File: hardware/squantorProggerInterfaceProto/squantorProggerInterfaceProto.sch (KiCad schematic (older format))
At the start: 2 parts

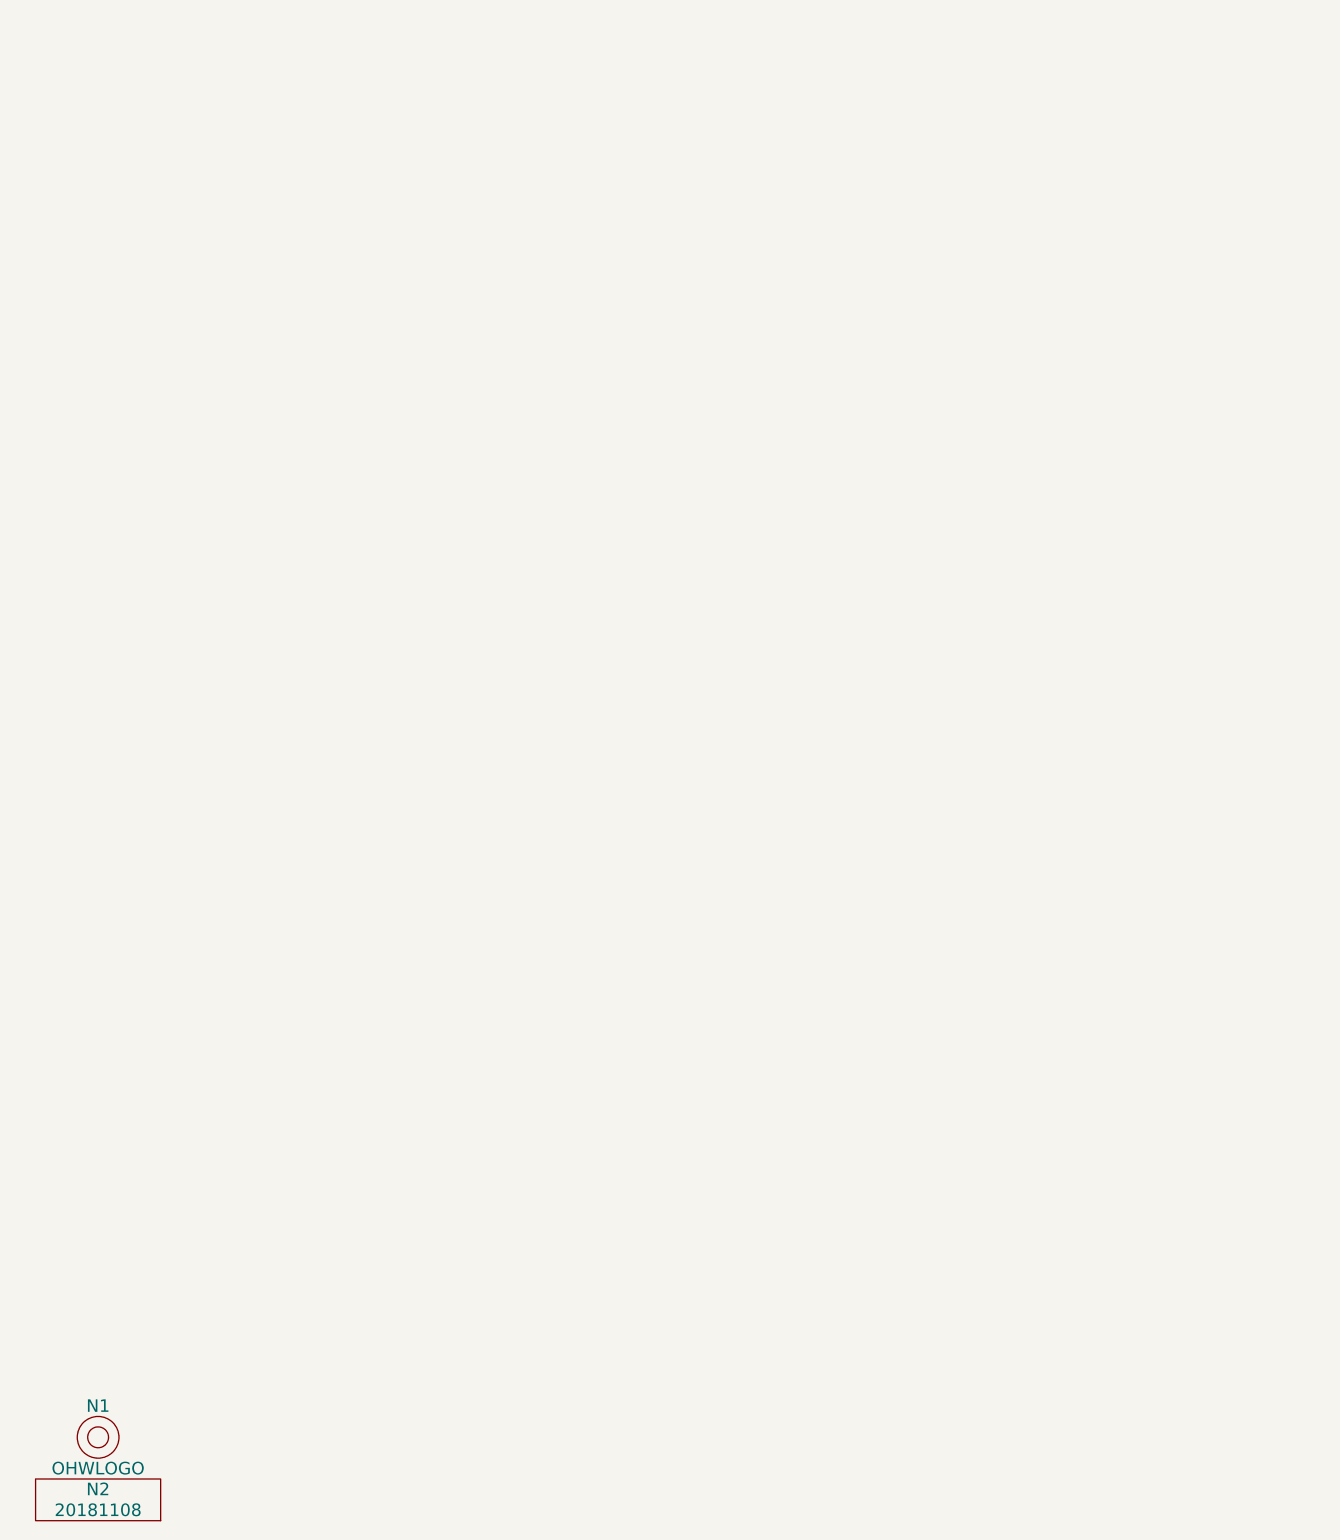
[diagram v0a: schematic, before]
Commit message: completed schematic, passes DRC
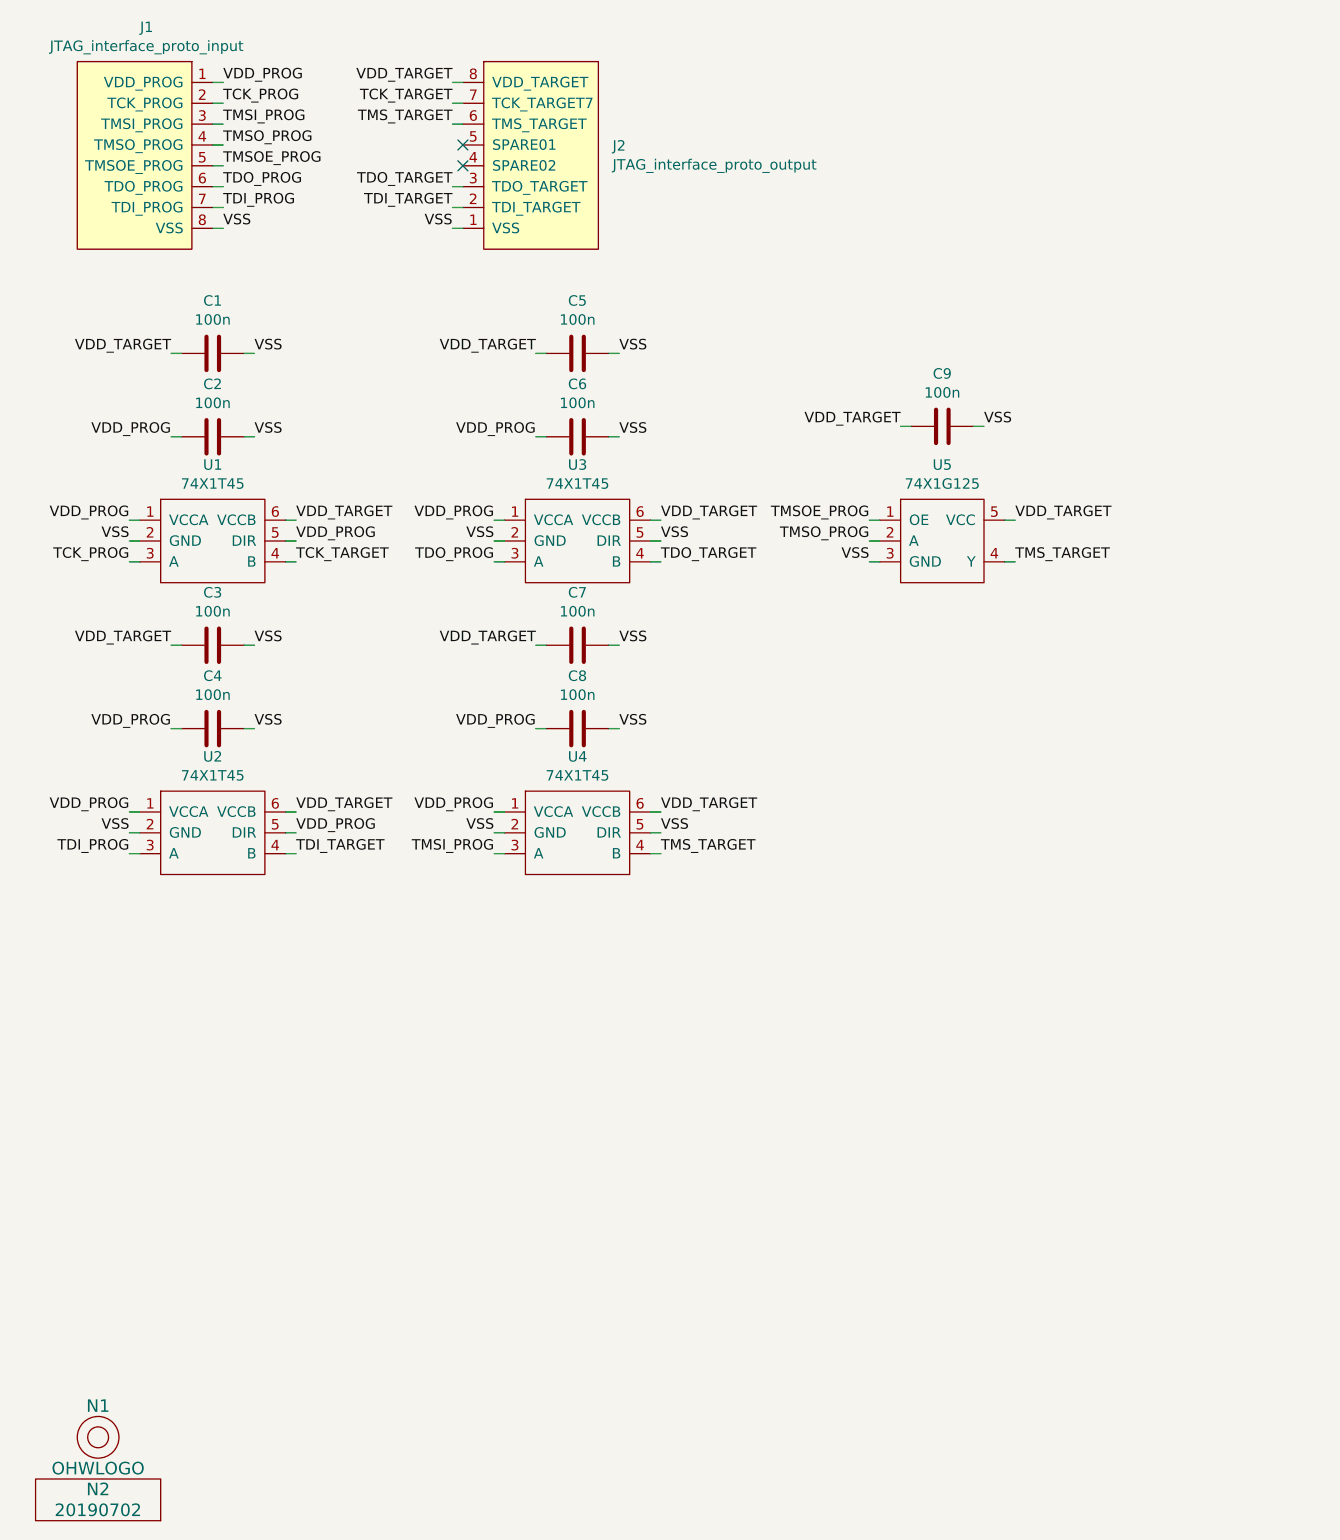
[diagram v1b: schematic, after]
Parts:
- added C1, C2, C3, C4, C5, C6, C7, C8, C9: 100n, SquantorRcl:C_0402, symbol Device:C
- added J1: JTAG_interface_proto_input, symbol SquantorConnectorsNamed:JTAG_interface_proto_input
- added J2: JTAG_interface_proto_output, symbol SquantorConnectorsNamed:JTAG_interface_proto_output
- added U1, U2, U3, U4: 74X1T45, symbol SquantorLogic:74X1T45
- added U5: 74X1G125, symbol SquantorLogic:74X1G125
- N2: value 20181108 -> 20190702
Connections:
- new net TCK_PROG: J1.2 (TCK_PROG), U1.3 (A)
- new net TCK_TARGET: J2.7 (TCK_TARGET7), U1.4 (B)
- new net TDI_PROG: J1.7 (TDI_PROG), U2.3 (A)
- new net TDI_TARGET: J2.2 (TDI_TARGET), U2.4 (B)
- new net TDO_PROG: J1.6 (TDO_PROG), U3.3 (A)
- new net TDO_TARGET: J2.3 (TDO_TARGET), U3.4 (B)
- new net TMSI_PROG: J1.3 (TMSI_PROG), U4.3 (A)
- new net TMSOE_PROG: J1.5 (TMSOE_PROG), U5.1 (OE)
- new net TMSO_PROG: J1.4 (TMSO_PROG), U5.2 (A)
- new net TMS_TARGET: J2.6 (TMS_TARGET), U4.4 (B), U5.4 (Y)
- new net VDD_PROG: C2.2, C4.2, C6.2, C8.2, J1.1 (VDD_PROG), U1.1 (VCCA), U1.5 (DIR), U2.1 (VCCA), U2.5 (DIR), U3.1 (VCCA), U4.1 (VCCA)
- new net VDD_TARGET: C1.2, C3.2, C5.2, C7.2, C9.2, J2.8 (VDD_TARGET), U1.6 (VCCB), U2.6 (VCCB), U3.6 (VCCB), U4.6 (VCCB), U5.5 (VCC)
- new net VSS: C1.1, C2.1, C3.1, C4.1, C5.1, C6.1, C7.1, C8.1, C9.1, J1.8 (VSS), J2.1 (VSS), U1.2 (GND), U2.2 (GND), U3.2 (GND), U3.5 (DIR), U4.2 (GND), U4.5 (DIR), U5.3 (GND)
- no-connect marks 0 -> 2

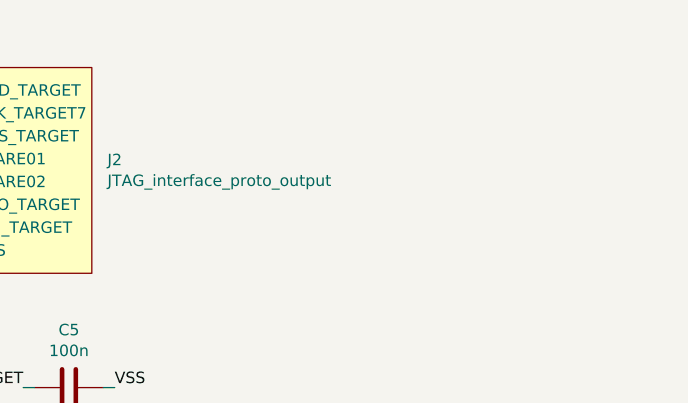
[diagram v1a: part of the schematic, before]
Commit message: added rail decoupling
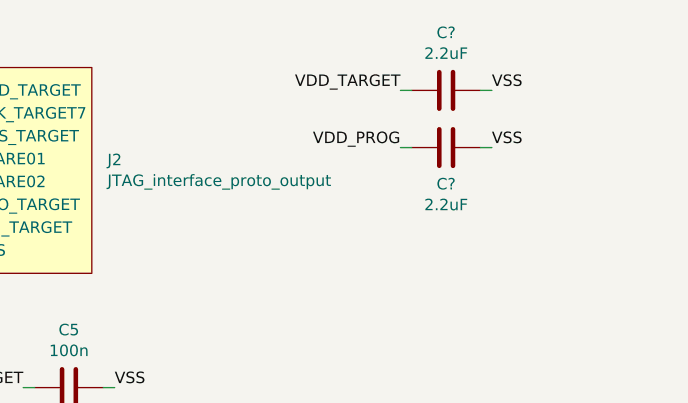
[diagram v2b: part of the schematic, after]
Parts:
- added C? (x2): 2.2uF, SquantorRcl:C_0805, symbol Device:C
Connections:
- net VDD_PROG: now also C?.2
- net VDD_TARGET: now also C?.2
- net VSS: now also C?.1, C?.1
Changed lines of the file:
@@
 Wire Wire Line
 	5200 2950 5250 2950
+$Comp
+L Device:C C?
+U 1 1 5D1D36E6
+P 4800 850
+F 0 "C?" V 4548 850 50  0000 C CNN
+F 1 "2.2uF" V 4639 850 50  0000 C CNN
+F 2 "SquantorRcl:C_0805" H 4838 700 50  0001 C CNN
+F 3 "~" H 4800 850 50  0001 C CNN
+	1    4800 850
+	0    1    1    0
+$EndComp
+$Comp
+L Device:C C?
+U 1 1 5D1D44ED
+P 4800 1100
+F 0 "C?" V 4960 1100 50  0000 C CNN
+F 1 "2.2uF" V 5051 1100 50  0000 C CNN
+F 2 "SquantorRcl:C_0805" H 4838 950 50  0001 C CNN
+F 3 "~" H 4800 1100 50  0001 C CNN
+	1    4800 1100
+	0    1    1    0
+$EndComp
+Text Label 5000 850  0    50   ~ 0
+VSS
+Text Label 5000 1100 0    50   ~ 0
+VSS
+Wire Wire Line
+	5000 850  4950 850
+Wire Wire Line
+	4950 1100 5000 1100
+Text Label 4600 850  2    50   ~ 0
+VDD_TARGET
+Text Label 4600 1100 2    50   ~ 0
+VDD_PROG
+Wire Wire Line
+	4600 850  4650 850
+Wire Wire Line
+	4650 1100 4600 1100
 $EndSCHEMATC

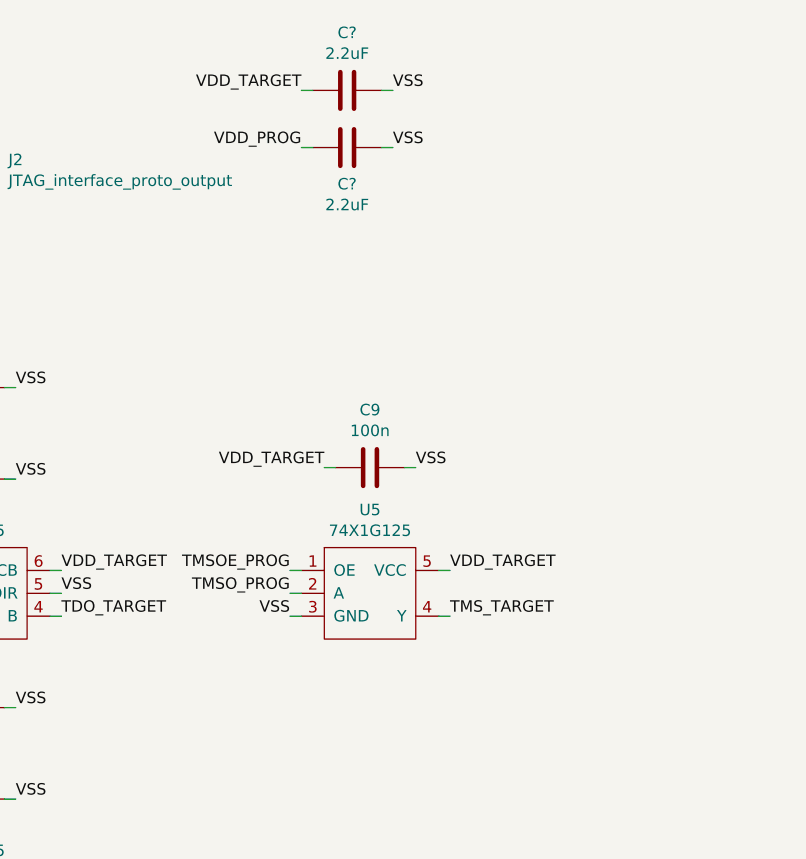
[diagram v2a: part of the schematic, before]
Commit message: footprints defined for level shifter IC's
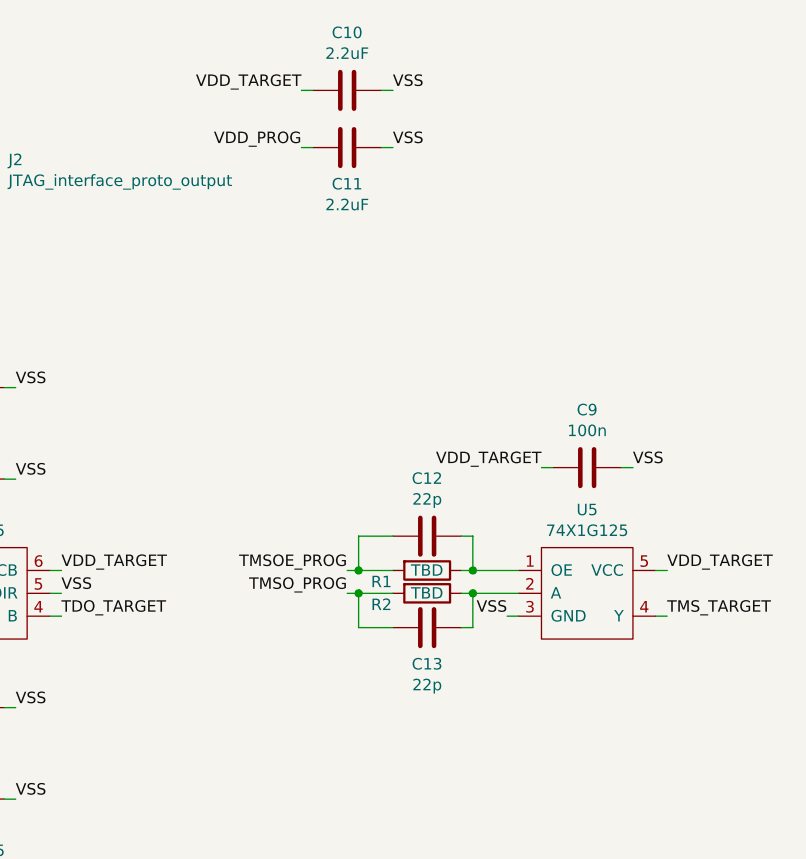
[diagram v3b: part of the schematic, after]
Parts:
- added C12, C13: 22p, SquantorRcl:C_0402, symbol Device:C
- added R1, R2: TBD, SquantorRcl:R_0402_hand, symbol Device:R
- U1, U2, U3, U4: footprint (none) -> SquantorIC:SOT363-hand
- U5: footprint (none) -> SquantorIC:SOT353-hand
- gave numbers to parts that had none: 2
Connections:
- net TMSOE_PROG: now also C12.2, R1.2; no longer U5.1 (OE)
- net TMSO_PROG: now also C13.2, R2.2; no longer U5.2 (A)
- new net: C12.1, R1.1, U5.1 (OE)
- new net: C13.1, R2.1, U5.2 (A)
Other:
- moved on the sheet: C9, U5
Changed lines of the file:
@@
 F 0 "U1" H 1400 3415 50  0000 C CNN
 F 1 "74X1T45" H 1400 3324 50  0000 C CNN
-F 2 "" H 1400 3050 50  0001 C CNN
+F 2 "SquantorIC:SOT363-hand" H 1400 3050 50  0001 C CNN
 F 3 "" H 1400 3050 50  0001 C CNN
 	1    1400 3050
@@
 F 0 "U2" H 1400 4815 50  0000 C CNN
 F 1 "74X1T45" H 1400 4724 50  0000 C CNN
-F 2 "" H 1400 4450 50  0001 C CNN
+F 2 "SquantorIC:SOT363-hand" H 1400 4450 50  0001 C CNN
 F 3 "" H 1400 4450 50  0001 C CNN
 	1    1400 4450
@@
 F 0 "U3" H 3150 3415 50  0000 C CNN
 F 1 "74X1T45" H 3150 3324 50  0000 C CNN
-F 2 "" H 3150 3050 50  0001 C CNN
+F 2 "SquantorIC:SOT363-hand" H 3150 3050 50  0001 C CNN
 F 3 "" H 3150 3050 50  0001 C CNN
 	1    3150 3050
@@
 F 0 "U4" H 3150 4815 50  0000 C CNN
 F 1 "74X1T45" H 3150 4724 50  0000 C CNN
-F 2 "" H 3150 4450 50  0001 C CNN
+F 2 "SquantorIC:SOT363-hand" H 3150 4450 50  0001 C CNN
 F 3 "" H 3150 4450 50  0001 C CNN
 	1    3150 4450
@@
 L SquantorLogic:74X1G125 U5
 U 1 1 5D1E9D88
-P 4900 3050
-F 0 "U5" H 4900 3415 50  0000 C CNN
-F 1 "74X1G125" H 4900 3324 50  0000 C CNN
-F 2 "" H 4900 3050 50  0001 C CNN
-F 3 "" H 4900 3050 50  0001 C CNN
-	1    4900 3050
-	1    0    0    -1
-$EndComp
-Text Label 5100 2500 0    50   ~ 0
+P 5850 3050
+F 0 "U5" H 5850 3415 50  0000 C CNN
+F 1 "74X1G125" H 5850 3324 50  0000 C CNN
+F 2 "SquantorIC:SOT353-hand" H 5850 3050 50  0001 C CNN
+F 3 "" H 5850 3050 50  0001 C CNN
+	1    5850 3050
+	1    0    0    -1
+$EndComp
+Text Label 6050 2500 0    50   ~ 0
 VSS
 $Comp
 L Device:C C9
 U 1 1 5D1EC165
-P 4900 2500
-F 0 "C9" V 4648 2500 50  0000 C CNN
-F 1 "100n" V 4739 2500 50  0000 C CNN
-F 2 "SquantorRcl:C_0402" H 4938 2350 50  0001 C CNN
-F 3 "~" H 4900 2500 50  0001 C CNN
-	1    4900 2500
-	0    1    1    0
-$EndComp
-Wire Wire Line
-	5100 2500 5050 2500
-Text Label 4700 2500 2    50   ~ 0
-VDD_TARGET
-Wire Wire Line
-	4750 2500 4700 2500
-Text Label 5250 2950 0    50   ~ 0
-VDD_TARGET
-Text Label 4550 3150 2    50   ~ 0
-VSS
-Wire Wire Line
-	4600 3150 4550 3150
-Wire Wire Line
-	5200 3150 5250 3150
-Wire Wire Line
-	4600 3050 4550 3050
-Wire Wire Line
-	4600 2950 4550 2950
-Text Label 4550 2950 2    50   ~ 0
+P 5850 2500
+F 0 "C9" V 5598 2500 50  0000 C CNN
+F 1 "100n" V 5689 2500 50  0000 C CNN
+F 2 "SquantorRcl:C_0402" H 5888 2350 50  0001 C CNN
+F 3 "~" H 5850 2500 50  0001 C CNN
+	1    5850 2500
+	0    1    1    0
+$EndComp
+Wire Wire Line
+	6050 2500 6000 2500
+Text Label 5650 2500 2    50   ~ 0
+VDD_TARGET
+Wire Wire Line
+	5700 2500 5650 2500
+Text Label 6200 2950 0    50   ~ 0
+VDD_TARGET
+Text Label 5500 3150 2    50   ~ 0
+VSS
+Wire Wire Line
+	5550 3150 5500 3150
+Wire Wire Line
+	6150 3150 6200 3150
+Text Label 4800 2950 2    50   ~ 0
 TMSOE_PROG
-Text Label 4550 3050 2    50   ~ 0
+Text Label 4800 3050 2    50   ~ 0
 TMSO_PROG
-Text Label 5250 3150 0    50   ~ 0
+Text Label 6200 3150 0    50   ~ 0
 TMS_TARGET
 $Comp
@@
 NoConn ~ 2600 1250
 Wire Wire Line
-	5200 2950 5250 2950
-$Comp
-L Device:C C?
+	6150 2950 6200 2950
+$Comp
+L Device:C C10
 U 1 1 5D1D36E6
 P 4800 850
-F 0 "C?" V 4548 850 50  0000 C CNN
+F 0 "C10" V 4548 850 50  0000 C CNN
 F 1 "2.2uF" V 4639 850 50  0000 C CNN
 F 2 "SquantorRcl:C_0805" H 4838 700 50  0001 C CNN
@@
 $EndComp
 $Comp
-L Device:C C?
+L Device:C C11
 U 1 1 5D1D44ED
 P 4800 1100
-F 0 "C?" V 4960 1100 50  0000 C CNN
+F 0 "C11" V 4960 1100 50  0000 C CNN
 F 1 "2.2uF" V 5051 1100 50  0000 C CNN
 F 2 "SquantorRcl:C_0805" H 4838 950 50  0001 C CNN
@@
 Wire Wire Line
 	4650 1100 4600 1100
+$Comp
+L Device:C C12
+U 1 1 5D1E5D02
+P 5150 2800
+F 0 "C12" V 4898 2800 50  0000 C CNN
+F 1 "22p" V 4989 2800 50  0000 C CNN
+F 2 "SquantorRcl:C_0402" H 5188 2650 50  0001 C CNN
+F 3 "~" H 5150 2800 50  0001 C CNN
+	1    5150 2800
+	0    1    1    0
+$EndComp
+$Comp
+L Device:R R1
+U 1 1 5D1E6AFD
+P 5150 2950
+F 0 "R1" V 5200 2750 50  0000 C CNN
+F 1 "TBD" V 5150 2950 50  0000 C CNN
+F 2 "SquantorRcl:R_0402_hand" V 5080 2950 50  0001 C CNN
+F 3 "~" H 5150 2950 50  0001 C CNN
+	1    5150 2950
+	0    1    1    0
+$EndComp
+$Comp
+L Device:R R2
+U 1 1 5D1E7071
+P 5150 3050
+F 0 "R2" V 5200 2850 50  0000 C CNN
+F 1 "TBD" V 5150 3050 50  0000 C CNN
+F 2 "SquantorRcl:R_0402_hand" V 5080 3050 50  0001 C CNN
+F 3 "~" H 5150 3050 50  0001 C CNN
+	1    5150 3050
+	0    1    1    0
+$EndComp
+$Comp
+L Device:C C13
+U 1 1 5D1E8518
+P 5150 3200
+F 0 "C13" V 5310 3200 50  0000 C CNN
+F 1 "22p" V 5401 3200 50  0000 C CNN
+F 2 "SquantorRcl:C_0402" H 5188 3050 50  0001 C CNN
+F 3 "~" H 5150 3200 50  0001 C CNN
+	1    5150 3200
+	0    1    1    0
+$EndComp
+Wire Wire Line
+	4800 2950 4850 2950
+Wire Wire Line
+	5300 2950 5350 2950
+Wire Wire Line
+	5300 3050 5350 3050
+Wire Wire Line
+	5000 3050 4850 3050
+Wire Wire Line
+	5000 3200 4850 3200
+Wire Wire Line
+	4850 3200 4850 3050
+Connection ~ 4850 3050
+Wire Wire Line
+	4850 3050 4800 3050
+Wire Wire Line
+	4850 2950 4850 2800
+Wire Wire Line
+	4850 2800 5000 2800
+Connection ~ 4850 2950
+Wire Wire Line
+	4850 2950 5000 2950
+Wire Wire Line
+	5300 2800 5350 2800
+Wire Wire Line
+	5350 2800 5350 2950
+Connection ~ 5350 2950
+Wire Wire Line
+	5350 2950 5550 2950
+Wire Wire Line
+	5350 3050 5350 3200
+Wire Wire Line
+	5350 3200 5300 3200
+Connection ~ 5350 3050
+Wire Wire Line
+	5350 3050 5550 3050
 $EndSCHEMATC

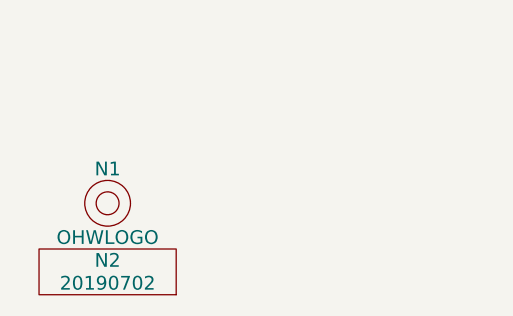
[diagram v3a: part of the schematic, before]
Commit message: initial placement of components
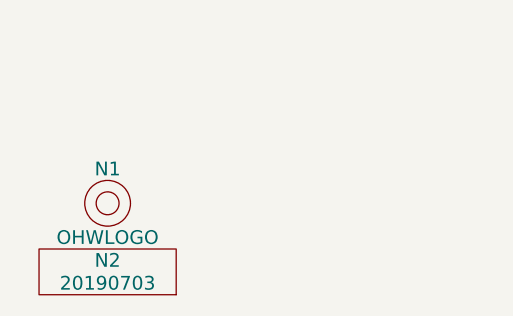
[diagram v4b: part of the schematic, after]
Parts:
- J1, J2: footprint (none) -> SquantorConnectors:Header-0254-1X08-H010
- N2: value 20190702 -> 20190703
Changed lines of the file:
@@
 P 850 7700
 F 0 "N2" H 850 7800 60  0000 C CNN
-F 1 "20190702" H 850 7700 60  0000 C CNN
+F 1 "20190703" H 850 7700 60  0000 C CNN
 F 2 "SquantorLabels:Label_version" H 850 7700 60  0001 C CNN
 F 3 "" H 850 7700 60  0001 C CNN
@@
 F 0 "J1" H 1083 2215 50  0000 C CNN
 F 1 "JTAG_interface_proto_input" H 1083 2124 50  0000 C CNN
-F 2 "" H 1100 1400 50  0001 C CNN
+F 2 "SquantorConnectors:Header-0254-1X08-H010" H 1100 1400 50  0001 C CNN
 F 3 "" H 1100 1400 50  0001 C CNN
 	1    1050 1400
@@
 F 0 "J2" H 2682 1046 50  0000 R CNN
 F 1 "JTAG_interface_proto_output" H 2682 955 50  0000 R CNN
-F 2 "" H 3000 1100 50  0001 C CNN
+F 2 "SquantorConnectors:Header-0254-1X08-H010" H 3000 1100 50  0001 C CNN
 F 3 "" H 3000 1100 50  0001 C CNN
 	1    3000 1100
